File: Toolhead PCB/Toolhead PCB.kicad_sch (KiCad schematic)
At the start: 10 parts, among them J1 SKR Pico 1, J10 BQ MicroProbe, J2 SKR Pico 2, J3 SKR Pico 3, J4 Hot End Heater, J5 Hot End Thermistor, J6 Heatbreak Fan, J7 Part Fan, J8 Part Fan 2, J9 Muon 3D IR+ADXL345

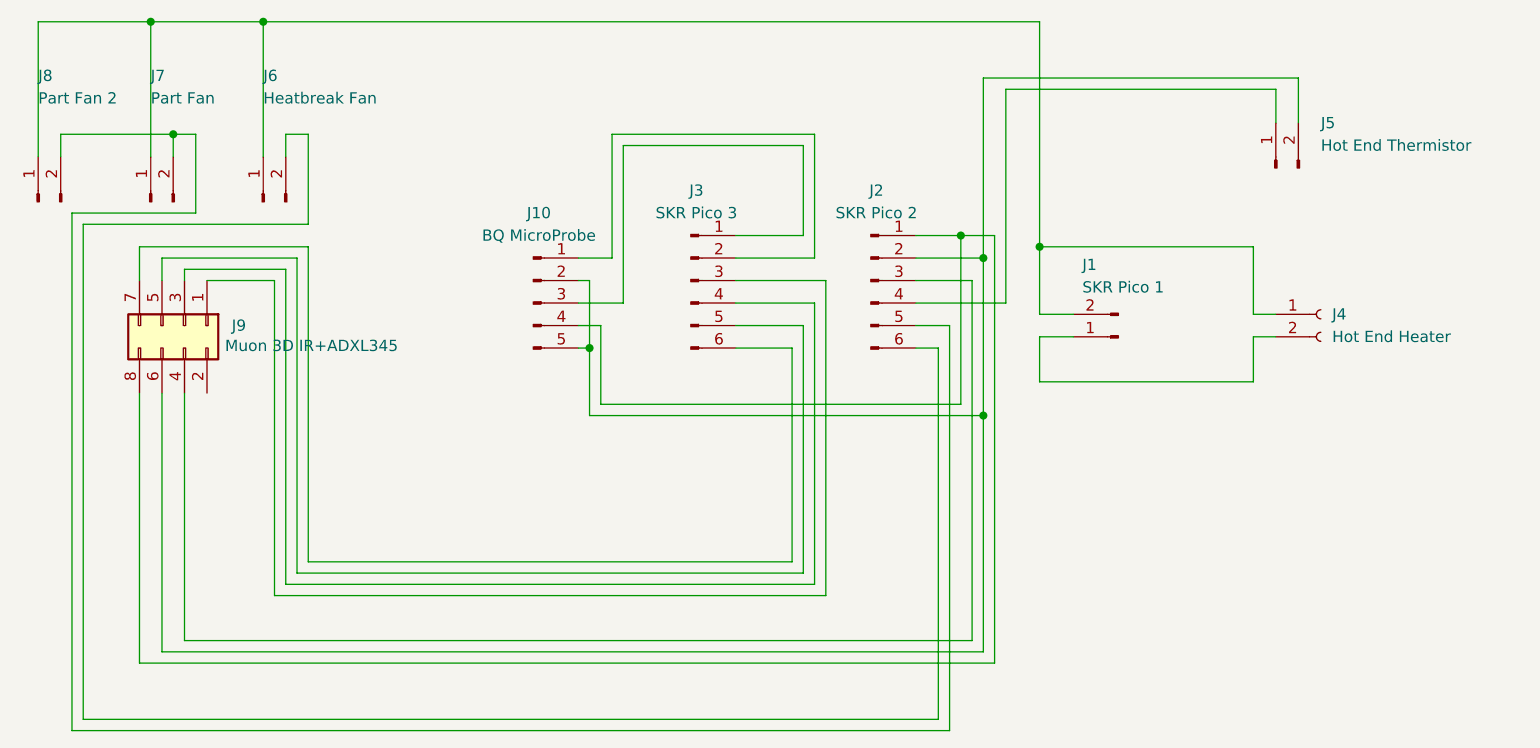
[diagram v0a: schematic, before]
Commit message: Schematic and PCB for JourneyMaker Toolhead PCB: - J1 Soldered wires from SKR Pico for Hot End Heater - J2 JST PH 2.0 6-pin from SKR Pico for BQ MicroProbe and Muon IR Probe's ADXL345 - J3 JST PH 2.0 6-pin from SKR Pico for Muon IR Bed Probe and Fans - J4 Amass XT30PW-F Hot End Heater - J5 JST XH Thermistor - J6 JST XH Heatbreak Fan - J7 JST XH Part Fan - J8 low profile header connector for the Muon IR Bed Probe and ADXL345 Accelerometer    - The low profile header reverse connects to the Muon PCB pins; PCB acts as an optical shield for the IR probe    - Special hole for the capacitor to let PCB be close - J9 JST PH 2.0 5-pin for the BQ MicroProbe
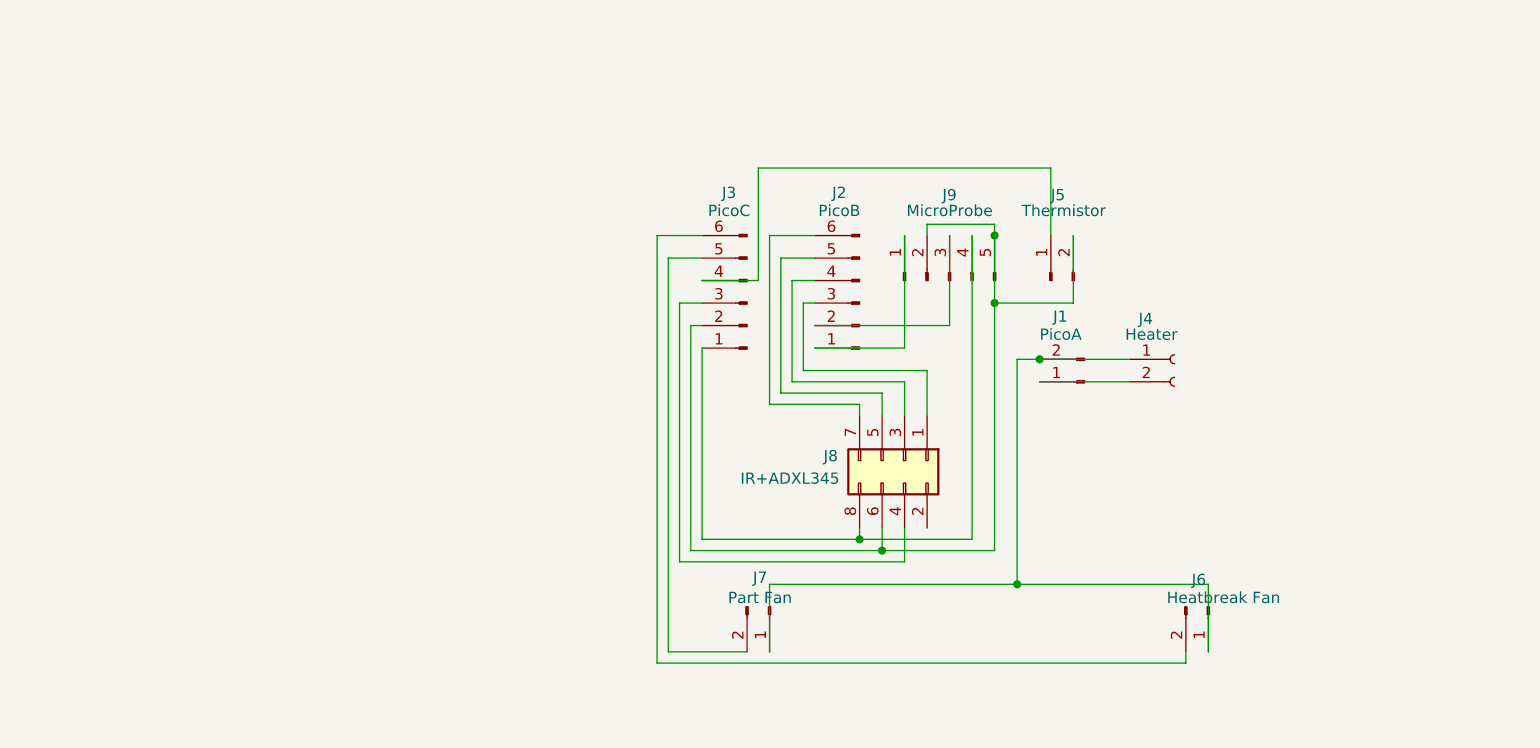
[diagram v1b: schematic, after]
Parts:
- removed J8: Part Fan 2, Connector_JST:JST_XH_B2B-XH-A_1x02_P2.50mm_Vertical, symbol Connector:Conn_01x02_Pin
- J1: value SKR Pico 1 -> PicoA; footprint Connector_AMASS:AMASS_XT30PW-M_1x02_P2.50mm_Horizontal -> TerminalBlock_Phoenix:TerminalBlock_Phoenix_MPT-0,5-2-2.54_1x02_P2.54mm_Horizontal
- J2: renamed from J3; value SKR Pico 3 -> PicoB; footprint Connector_JST:JST_PH_S6B-PH-K_1x06_P2.00mm_Horizontal -> Connector_JST:JST_PH_B6B-PH-K_1x06_P2.00mm_Vertical
- J3: renamed from J2; value SKR Pico 2 -> PicoC; footprint Connector_JST:JST_PH_S6B-PH-K_1x06_P2.00mm_Horizontal -> Connector_JST:JST_PH_B6B-PH-K_1x06_P2.00mm_Vertical
- J4: value Hot End Heater -> Heater
- J5: value Hot End Thermistor -> Thermistor
- J8: renamed from J9; value Muon 3D IR+ADXL345 -> IR+ADXL345
- J9: renamed from J10; value BQ MicroProbe -> MicroProbe
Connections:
- net at J9.1 (Pin_1): now also J2.1 (Pin_1); no longer J2.2 (Pin_2)
- net at J9.3 (Pin_3): now also J2.2 (Pin_2); no longer J2.1 (Pin_1)
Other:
- moved on the sheet: J1, J2, J3, J4, J5, J6, J7, J8, J9

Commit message: Used wider traces for heater, fans, thermistor, microprobe power, etc.
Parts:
- J1: footprint TerminalBlock_Phoenix:TerminalBlock_Phoenix_MPT-0,5-2-2.54_1x02_P2.54mm_Horizontal -> TerminalBlock:TerminalBlock_Xinya_XY308-2.54-2P_1x02_P2.54mm_Horizontal
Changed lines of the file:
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@@
 			)
 		)
-		(property "Footprint" "TerminalBlock_Phoenix:TerminalBlock_Phoenix_MPT-0,5-2-2.54_1x02_P2.54mm_Horizontal"
+		(property "Footprint" "TerminalBlock:TerminalBlock_Xinya_XY308-2.54-2P_1x02_P2.54mm_Horizontal"
 			(at 159.385 115.57 0)
 			(effects

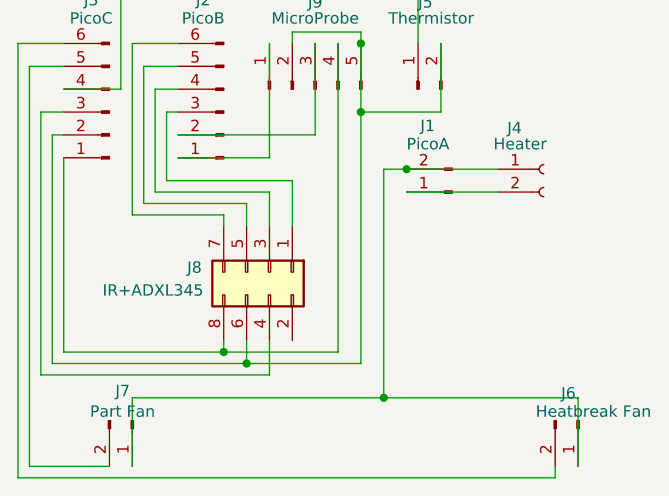
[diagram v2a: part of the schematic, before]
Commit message: Combine a through-hole and an SMD connector to get the passthrough holes and vias.
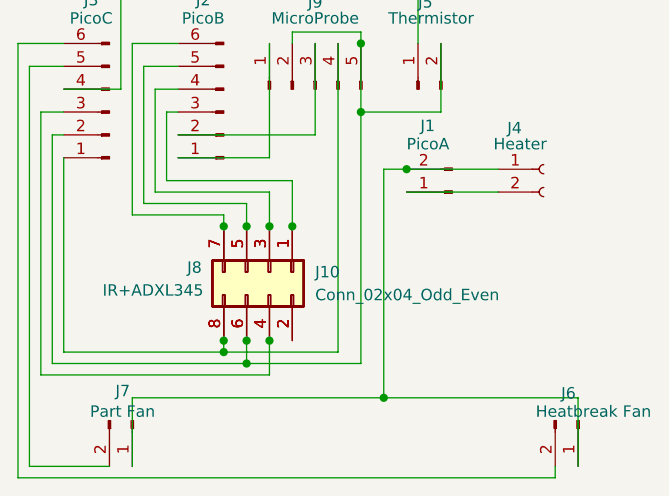
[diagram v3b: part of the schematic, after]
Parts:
- added J10: Conn_02x04_Odd_Even, Connector_PinHeader_2.54mm:PinHeader_2x04_P2.54mm_Vertical, symbol Connector_Generic:Conn_02x04_Odd_Even
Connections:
- net at J3.2 (Pin_2), J5.2 (Pin_2), J8.6 (Pin_6)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: now also J10.6 (Pin_6)
- net at J3.1 (Pin_1), J8.8 (Pin_8), J9.4 (Pin_4): now also J10.8 (Pin_8)
- net at J2.3 (Pin_3), J8.1 (Pin_1): now also J10.1 (Pin_1)
- net at J2.4 (Pin_4), J8.3 (Pin_3): now also J10.3 (Pin_3)
- net at J2.5 (Pin_5), J8.5 (Pin_5): now also J10.5 (Pin_5)
- net at J2.6 (Pin_6), J8.7 (Pin_7): now also J10.7 (Pin_7)
- net at J3.3 (Pin_3), J8.4 (Pin_4): now also J10.4 (Pin_4)
- net at J8.2 (Pin_2): now also J10.2 (Pin_2)
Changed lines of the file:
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@@
+	)
+	(junction
+		(at 137.16 116.84)
+		(diameter 0)
+		(color 0 0 0 0)
 	)
 	(junction
@@
 	)
 	(junction
+		(at 134.62 129.54)
+		(diameter 0)
+		(color 0 0 0 0)
+	)
+	(junction
+		(at 134.62 116.84)
+		(diameter 0)
+		(color 0 0 0 0)
+	)
+	(junction
+		(at 139.7 116.84)
+		(diameter 0)
+		(color 0 0 0 0)
+	)
+	(junction
 		(at 137.16 132.08)
 		(diameter 0)
@@
 	)
 	(junction
+		(at 139.7 129.54)
+		(diameter 0)
+		(color 0 0 0 0)
+	)
+	(junction
 		(at 149.86 96.52)
 		(diameter 0)
@@
 	)
 	(junction
+		(at 137.16 129.54)
+		(diameter 0)
+		(color 0 0 0 0)
+	)
+	(junction
+		(at 142.24 116.84)
+		(diameter 0)
+		(color 0 0 0 0)
+	)
+	(junction
 		(at 152.4 135.89)
 		(diameter 0)
@@
 	(wire
 		(pts
+			(xy 152.4 110.49) (xy 152.4 135.89)
+		)
+		(stroke
+			(width 0)
+			(type default)
+		)
+	)
+	(wire
+		(pts
 			(xy 111.76 96.52) (xy 111.76 144.78)
 		)
@@
 		(pts
 			(xy 134.62 130.81) (xy 134.62 129.54)
-		)
-		(stroke
-			(width 0)
-			(type default)
-		)
-	)
-	(wire
-		(pts
-			(xy 152.4 110.49) (xy 152.4 135.89)
 		)
 		(stroke
@@
 					(unit 1)
 				)
+			)
+		)
+	)
+	(symbol
+		(lib_id "Connector_Generic:Conn_02x04_Odd_Even")
+		(at 139.7 121.92 270)
+		(unit 1)
+		(exclude_from_sim no)
+		(in_bom yes)
+		(on_board yes)
+		(dnp no)
+		(fields_autoplaced yes)
+		(property "Reference" "J10"
+			(at 144.78 121.9199 90)
+			(effects
+				(font
+					(size 1.27 1.27)
+				)
+				(justify left)
+			)
+		)
+		(property "Value" "Conn_02x04_Odd_Even"
+			(at 144.78 124.4599 90)
+			(effects
+				(font
+					(size 1.27 1.27)
+				)
+				(justify left)
+			)
+		)
+		(property "Footprint" "Connector_PinHeader_2.54mm:PinHeader_2x04_P2.54mm_Vertical"
+			(at 139.7 121.92 0)
+			(effects
+				(font
+					(size 1.27 1.27)
+				)
+				(hide yes)
+			)
+		)
+		(property "Datasheet" "~"
+			(at 139.7 121.92 0)
+			(effects
+				(font
+					(size 1.27 1.27)
+				)
+				(hide yes)
+			)
+		)
+		(property "Description" "Generic connector, double row, 02x04, odd/even pin numbering scheme (row 1 odd numbers, row 2 even numbers), script generated (kicad-library-utils/schlib/autogen/connector/)"
+			(at 139.7 121.92 0)
+			(effects
+				(font
+					(size 1.27 1.27)
+				)
+				(hide yes)
+			)
+		)
+		(pin "1"
+		)
+		(pin "7"
+		)
+		(pin "2"
+		)
+		(pin "6"
+		)
+		(pin "8"
+		)
+		(pin "4"
+		)
+		(pin "5"
+		)
+		(pin "3"
+		)
+		(instances
+			(project ""
+				(path "/c0597a7a-3bdb-4319-b43c-dc7e5bba73b5"
+					(reference "J10")
+					(unit 1)
+				)

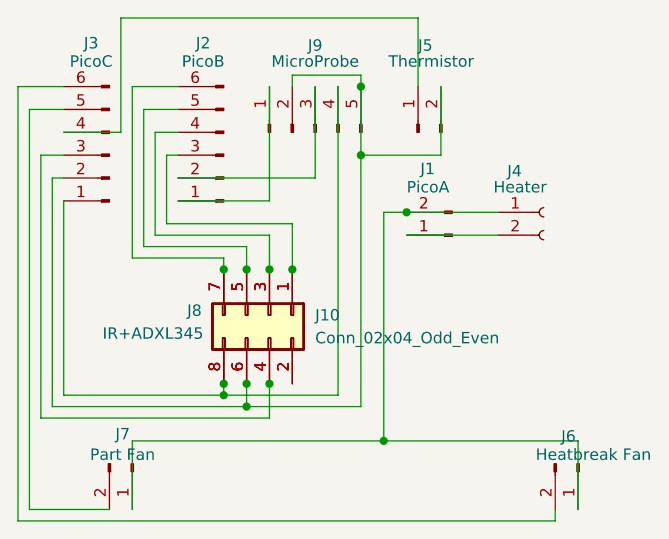
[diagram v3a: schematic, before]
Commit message: Holes for mounting. Moved traces to avoid holes. Moved most vias to the large pads. Changed the ADXLL345 wire order so it would route better. Made Schematic match PCB.
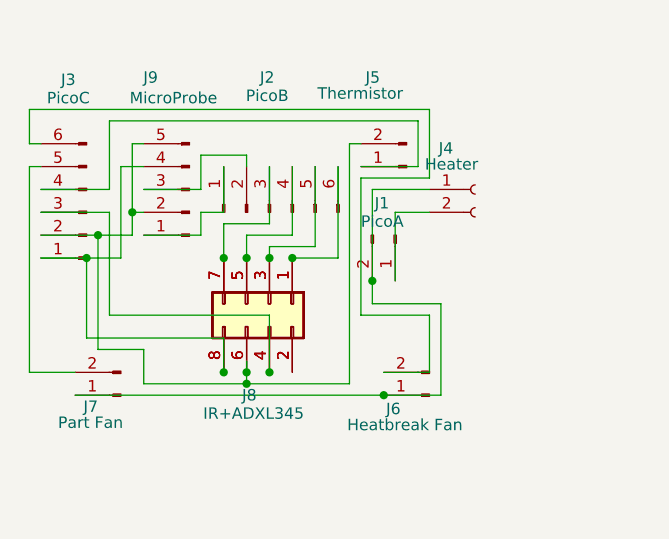
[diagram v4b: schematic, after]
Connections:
- net at J10.1 (Pin_1), J8.1 (Pin_1): now also J2.6 (Pin_6); no longer J2.3 (Pin_3)
- net at J10.3 (Pin_3), J8.3 (Pin_3): now also J2.5 (Pin_5); no longer J2.4 (Pin_4)
- net at J10.5 (Pin_5), J8.5 (Pin_5): now also J2.4 (Pin_4); no longer J2.5 (Pin_5)
- net at J10.7 (Pin_7), J8.7 (Pin_7): now also J2.3 (Pin_3); no longer J2.6 (Pin_6)
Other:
- company: (none) -> Colin Ng
- moved on the sheet: J1, J2, J3, J4, J5, J6, J7, J8, J9

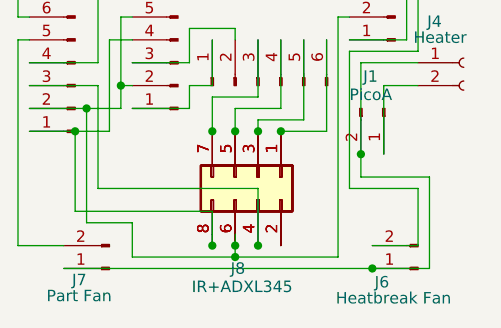
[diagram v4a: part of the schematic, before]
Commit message: Shortened label on IR+ADXL345 --> IR/ADXL Set the IR/ADXL header to Do Not Populate, and Exclude from BOM
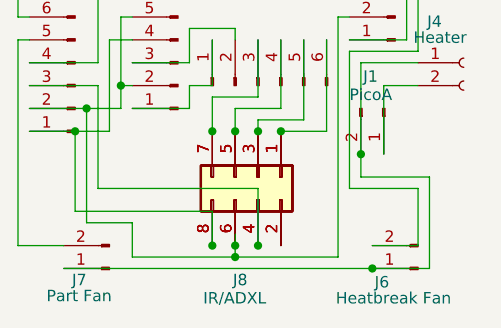
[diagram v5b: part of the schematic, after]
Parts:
- J8: value IR+ADXL345 -> IR/ADXL
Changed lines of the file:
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@@
 		(dnp no)
 		(property "Reference" "J8"
-			(at 136.652 130.81 90)
+			(at 136.906 132.08 90)
 			(effects
 				(font
@@
 			)
 		)
-		(property "Value" "IR+ADXL345"
-			(at 132.334 132.842 90)
+		(property "Value" "IR/ADXL"
+			(at 133.604 134.112 90)
 			(effects
 				(font

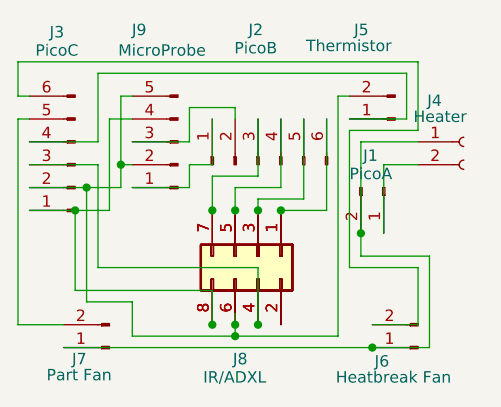
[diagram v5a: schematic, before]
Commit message: Created symbol and footprint for the Muon 3D IR Bed Probe with ADXL345.
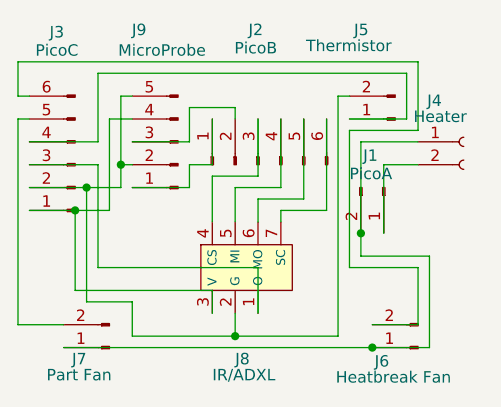
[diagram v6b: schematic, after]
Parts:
- removed J10: Conn_02x04_Odd_Even, Connector_PinHeader_2.54mm:PinHeader_2x04_P2.54mm_Vertical, symbol Connector_Generic:Conn_02x04_Odd_Even
- removed J8: IR/ADXL, Connector_PinHeader_2.54mm:PinHeader_2x04_P2.54mm_Vertical_SMD, symbol Connector_Generic:Conn_02x04_Odd_Even
- added J8: IR/ADXL, Positron V3:Muon 3D IR Bed Probe with ADXL345, symbol Positron V3:Muon3D_IR/ADXL_v2
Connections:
- net at J3.2 (Pin_2), J5.2 (Pin_2), J9.2 (Pin_2)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: now also J8.2 (G)
- net at J3.1 (Pin_1), J9.4 (Pin_4): now also J8.3 (V)
- net at J2.3 (Pin_3): now also J8.4 (CS)
- net at J2.4 (Pin_4): now also J8.5 (MI)
- net at J2.5 (Pin_5): now also J8.6 (MO)
- net at J2.6 (Pin_6): now also J8.7 (SC)
- net at J3.3 (Pin_3): now also J8.1 (O)
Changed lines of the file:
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@@
-	)
-	(junction
-		(at 139.7 115.57)
-		(diameter 0)
-		(color 0 0 0 0)
-	)
-	(junction
-		(at 137.16 115.57)
-		(diameter 0)
-		(color 0 0 0 0)
-	)
-	(junction
-		(at 134.62 115.57)
-		(diameter 0)
-		(color 0 0 0 0)
 	)
 	(junction
@@
 	)
 	(junction
-		(at 142.24 115.57)
-		(diameter 0)
-		(color 0 0 0 0)
-	)
-	(junction
 		(at 137.16 129.54)
 		(diameter 0)
@@
 	)
 	(junction
-		(at 134.62 128.27)
-		(diameter 0)
-		(color 0 0 0 0)
-	)
-	(junction
-		(at 139.7 128.27)
-		(diameter 0)
-		(color 0 0 0 0)
-	)
-	(junction
 		(at 151.13 118.11)
 		(diameter 0)
@@
 		(color 0 0 0 0)
 	)
-	(junction
-		(at 137.16 128.27)
-		(diameter 0)
-		(color 0 0 0 0)
-	)
 	(wire
 		(pts
@@
 	(wire
 		(pts
-			(xy 134.62 127) (xy 134.62 128.27)
-		)
-		(stroke
-			(width 0)
-			(type default)
-		)
-	)
-	(wire
-		(pts
 			(xy 121.92 100.33) (xy 156.21 100.33)
 		)
@@
 	(wire
 		(pts
+			(xy 137.16 113.03) (xy 137.16 116.84)
+		)
+		(stroke
+			(width 0)
+			(type default)
+		)
+	)
+	(wire
+		(pts
 			(xy 121.92 100.33) (xy 121.92 107.95)
 		)
@@
 	(wire
 		(pts
-			(xy 139.7 121.92) (xy 139.7 128.27)
+			(xy 139.7 121.92) (xy 139.7 127)
 		)
 		(stroke
@@
 	(wire
 		(pts
-			(xy 139.7 114.3) (xy 139.7 115.57)
-		)
-		(stroke
-			(width 0)
-			(type default)
-		)
-	)
-	(wire
-		(pts
-			(xy 137.16 127) (xy 137.16 128.27)
+			(xy 139.7 114.3) (xy 139.7 116.84)
+		)
+		(stroke
+			(width 0)
+			(type default)
+		)
+	)
+	(wire
+		(pts
+			(xy 137.16 127) (xy 137.16 129.54)
 		)
 		(stroke
@@
 	(wire
 		(pts
-			(xy 137.16 128.27) (xy 137.16 129.54)
-		)
-		(stroke
-			(width 0)
-			(type default)
-			(color 0 0 0 1)
-		)
-	)
-	(wire
-		(pts
 			(xy 120.65 113.03) (xy 124.46 113.03)
 		)
@@
 	(wire
 		(pts
-			(xy 134.62 111.76) (xy 134.62 115.57)
+			(xy 142.24 115.57) (xy 142.24 116.84)
+		)
+		(stroke
+			(width 0)
+			(type default)
+		)
+	)
+	(wire
+		(pts
+			(xy 134.62 111.76) (xy 134.62 116.84)
 		)
 		(stroke
@@
 		(pts
 			(xy 114.3 105.41) (xy 113.03 105.41)
-		)
-		(stroke
-			(width 0)
-			(type default)
-		)
-	)
-	(wire
-		(pts
-			(xy 137.16 113.03) (xy 137.16 115.57)
 		)
 		(stroke
@@
 	)
 	(symbol
-		(lib_id "Connector_Generic:Conn_02x04_Odd_Even")
-		(at 139.7 120.65 270)
-		(unit 1)
-		(exclude_from_sim no)
-		(in_bom yes)
-		(on_board yes)
-		(dnp no)
-		(fields_autoplaced yes)
-		(property "Reference" "J10"
-			(at 144.78 120.6499 90)
-			(effects
-				(font
-					(size 1.27 1.27)
-				)
-				(justify left)
-				(hide yes)
-			)
-		)
-		(property "Value" "Conn_02x04_Odd_Even"
-			(at 144.78 123.1899 90)
-			(effects
-				(font
-					(size 1.27 1.27)
-				)
-				(justify left)
-				(hide yes)
-			)
-		)
-		(property "Footprint" "Connector_PinHeader_2.54mm:PinHeader_2x04_P2.54mm_Vertical"
-			(at 139.7 120.65 0)
-			(effects
-				(font
-					(size 1.27 1.27)
-				)
-				(hide yes)
-			)
-		)
-		(property "Datasheet" "~"
-			(at 139.7 120.65 0)
-			(effects
-				(font
-					(size 1.27 1.27)
-				)
-				(hide yes)
-			)
-		)
-		(property "Description" "Generic connector, double row, 02x04, odd/even pin numbering scheme (row 1 odd numbers, row 2 even numbers), script generated (kicad-library-utils/schlib/autogen/connector/)"
-			(at 139.7 120.65 0)
-			(effects
-				(font
-					(size 1.27 1.27)
-				)
-				(hide yes)
-			)
-		)
-		(pin "1"
-		)
-		(pin "7"
-		)
-		(pin "2"
-		)
-		(pin "6"
-		)
-		(pin "8"
-		)
-		(pin "4"
-		)
-		(pin "5"
-		)
-		(pin "3"
-		)
-		(instances
-			(project ""
-				(path "/c0597a7a-3bdb-4319-b43c-dc7e5bba73b5"
-					(reference "J10")
-					(unit 1)
-				)
-			)
-		)
-	)
-	(symbol
 		(lib_id "Connector:Conn_01x02_Pin")
 		(at 157.48 130.81 180)
@@
 	)
 	(symbol
-		(lib_id "Connector_Generic:Conn_02x04_Odd_Even")
-		(at 139.7 120.65 270)
+		(lib_name "Muon3D_IR/ADXL_v2_1")
+		(lib_id "Positron V3:Muon3D_IR/ADXL_v2")
+		(at 138.43 114.3 0)
 		(unit 1)
 		(exclude_from_sim no)
@@
 		(dnp no)
 		(property "Reference" "J8"
-			(at 136.906 132.08 90)
+			(at 137.16 132.08 0)
 			(effects
 				(font
@@
 		)
 		(property "Value" "IR/ADXL"
-			(at 133.604 134.112 90)
+			(at 134.62 133.858 0)
 			(effects
 				(font
@@
 			)
 		)
-		(property "Footprint" "Connector_PinHeader_2.54mm:PinHeader_2x04_P2.54mm_Vertical_SMD"
-			(at 139.7 120.65 0)
-			(effects
-				(font
-					(size 1.27 1.27)
-				)
-				(hide yes)
-			)
-		)
-		(property "Datasheet" "~"
-			(at 139.7 120.65 0)
-			(effects
-				(font
-					(size 1.27 1.27)
-				)
-				(hide yes)
-			)
-		)
-		(property "Description" "Generic connector, double row, 02x04, odd/even pin numbering scheme (row 1 odd numbers, row 2 even numbers), script generated (kicad-library-utils/schlib/autogen/connector/)"
-			(at 139.7 120.65 0)
-			(effects
-				(font
-					(size 1.27 1.27)
-				)
-				(hide yes)
-			)
+		(property "Footprint" "Positron V3:Muon 3D IR Bed Probe with ADXL345"
+			(at 135.89 110.49 0)
+			(effects
+				(font
+					(size 1.27 1.27)
+				)
+				(hide yes)
+			)
+		)
+		(property "Datasheet" ""
+			(at 135.89 110.49 0)
+			(effects
+				(font
+					(size 1.27 1.27)
+				)
+				(hide yes)
+			)
+		)
+		(property "Description" ""
+			(at 135.89 110.49 0)
+			(effects
+				(font
+					(size 1.27 1.27)
+				)
+				(hide yes)
+			)
+		)
+		(pin "4"
+		)
+		(pin "3"
+		)
+		(pin "5"
+		)
+		(pin "2"
+		)
+		(pin "6"
 		)
 		(pin "1"
 		)
-		(pin "3"
-		)
-		(pin "5"
-		)
 		(pin "7"
 		)
-		(pin "2"
-		)
-		(pin "4"
-		)
-		(pin "6"
-		)
-		(pin "8"
-		)
 		(instances
